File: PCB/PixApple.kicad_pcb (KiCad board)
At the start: 2 copper layers, 100 x 100 mm, 0 parts

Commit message: Routing PCB
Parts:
- added C1: 10u, Capacitor_SMD:C_0603_1608Metric_Pad1.08x0.95mm_HandSolder, F.Cu at (203.7, 97.6)
- added C10: 1u, Capacitor_SMD:C_0603_1608Metric_Pad1.08x0.95mm_HandSolder, F.Cu at (98.1, 76.5)
- added C11: 1u, Capacitor_SMD:C_0603_1608Metric_Pad1.08x0.95mm_HandSolder, F.Cu at (90.0, 74.0)
- added C12: 100n, Capacitor_SMD:C_0603_1608Metric_Pad1.08x0.95mm_HandSolder, F.Cu at (112.1, 91.8)
- added C13: 100n, Capacitor_SMD:C_0603_1608Metric_Pad1.08x0.95mm_HandSolder, F.Cu at (101.4, 87.0)
- added C14: 100n, Capacitor_SMD:C_0603_1608Metric_Pad1.08x0.95mm_HandSolder, F.Cu at (193.8, 107.8)
- added C15: 15p, Capacitor_SMD:C_0603_1608Metric_Pad1.08x0.95mm_HandSolder, F.Cu at (193.6, 132.3)
- added C16: 15p, Capacitor_SMD:C_0603_1608Metric_Pad1.08x0.95mm_HandSolder, F.Cu at (193.6, 127.3)
- added C17: 100n, Capacitor_SMD:C_0603_1608Metric_Pad1.08x0.95mm_HandSolder, F.Cu at (99.9, 108.0)
- added C18: 100n, Capacitor_SMD:C_0603_1608Metric_Pad1.08x0.95mm_HandSolder, F.Cu at (219.4, 117.8)
- added C19: 30p, Capacitor_SMD:C_0603_1608Metric_Pad1.08x0.95mm_HandSolder, F.Cu at (105.5, 100.3)
- added C2: 10u, Capacitor_SMD:C_0603_1608Metric_Pad1.08x0.95mm_HandSolder, F.Cu at (208.1, 101.9)
- added C20: 30p, Capacitor_SMD:C_0603_1608Metric_Pad1.08x0.95mm_HandSolder, F.Cu at (105.5, 102.8)
- added C21: 4.7n, Capacitor_SMD:C_0603_1608Metric_Pad1.08x0.95mm_HandSolder, F.Cu at (227.2, 135.7)
- added C22: 100n, Capacitor_SMD:C_0603_1608Metric_Pad1.08x0.95mm_HandSolder, F.Cu at (239.2, 128.1)
- added C23: 1u, Capacitor_SMD:C_0603_1608Metric_Pad1.08x0.95mm_HandSolder, F.Cu at (240.8, 128.1)
- added C24: 100n, Capacitor_SMD:C_0603_1608Metric_Pad1.08x0.95mm_HandSolder, F.Cu at (219.4, 121.0)
- added C25: 1n, Capacitor_SMD:C_0603_1608Metric_Pad1.08x0.95mm_HandSolder, F.Cu at (219.4, 119.4)
- added C3: 100n, Capacitor_SMD:C_0603_1608Metric_Pad1.08x0.95mm_HandSolder, F.Cu at (105.5, 75.8)
- added C4: 100n, Capacitor_SMD:C_0603_1608Metric_Pad1.08x0.95mm_HandSolder, F.Cu at (111.8, 78.8)
- added C5: 100n, Capacitor_SMD:C_0603_1608Metric_Pad1.08x0.95mm_HandSolder, F.Cu at (97.4, 82.5)
- added C6: 100n, Capacitor_SMD:C_0603_1608Metric_Pad1.08x0.95mm_HandSolder, F.Cu at (103.9, 69.2)
- added C7: 100n, Capacitor_SMD:C_0603_1608Metric_Pad1.08x0.95mm_HandSolder, F.Cu at (96.2, 89.2)
- added C8: 100n, Capacitor_SMD:C_0603_1608Metric_Pad1.08x0.95mm_HandSolder, F.Cu at (101.5, 101.2)
- added C9: 100n, Capacitor_SMD:C_0603_1608Metric_Pad1.08x0.95mm_HandSolder, F.Cu at (111.6, 85.5)
- added D1: 1N4148W, Diode_SMD:D_SOD-123, F.Cu at (223.6, 118.2)
- added D2: LED_Small, LED_SMD:LED_0603_1608Metric_Pad1.05x0.95mm_HandSolder, F.Cu at (134.5, 123.5)
- added D3: LED_Small, LED_SMD:LED_0603_1608Metric_Pad1.05x0.95mm_HandSolder, F.Cu at (135.9, 134.0)
- added J1: USB_C_Receptacle_USB2.0_16P, Connector_USB:USB_C_Plug_Molex_105444, F.Cu at (189.2, 86.0)
- added J10: PWM0, Connector_PinHeader_2.54mm:PinHeader_1x03_P2.54mm_Vertical, F.Cu at (270.6, 84.0)
- added J11: PWM1, Connector_PinHeader_2.54mm:PinHeader_1x03_P2.54mm_Vertical, F.Cu at (270.6, 78.5)
- added J12: PWM2, Connector_PinHeader_2.54mm:PinHeader_1x03_P2.54mm_Vertical, F.Cu at (270.6, 73.0)
- added J13: PWM3, Connector_PinHeader_2.54mm:PinHeader_1x03_P2.54mm_Vertical, F.Cu at (270.6, 67.5)
- added J14: Conn_01x03_Pin, Connector_PinHeader_2.54mm:PinHeader_1x03_P2.54mm_Vertical, F.Cu at (25.0, 131.2)
- added J15: Conn_01x03_Pin, Connector_PinHeader_2.54mm:PinHeader_1x03_P2.54mm_Vertical, F.Cu at (25.0, 125.0)
- added J16: Conn_01x03_Pin, Connector_PinHeader_2.54mm:PinHeader_1x03_P2.54mm_Vertical, F.Cu at (34.7, 148.0)
- added J17: Conn_01x03_Pin, Connector_PinHeader_2.54mm:PinHeader_1x03_P2.54mm_Vertical, F.Cu at (34.7, 143.4)
- added J18: Conn_01x03_Pin, Connector_PinHeader_2.54mm:PinHeader_1x03_P2.54mm_Vertical, F.Cu at (34.7, 138.8)
- added J19: Conn_01x03_Pin, Connector_PinHeader_2.54mm:PinHeader_1x03_P2.54mm_Vertical, F.Cu at (34.7, 134.2)
- added J2: Conn_01x02_Pin, Connector_PinHeader_2.54mm:PinHeader_1x02_P2.54mm_Vertical, F.Cu at (185.8, 96.2)
- added J20: Conn_01x03_Pin, Connector_PinHeader_2.54mm:PinHeader_1x03_P2.54mm_Vertical, F.Cu at (34.7, 129.6)
- added J21: Conn_01x03_Pin, Connector_PinHeader_2.54mm:PinHeader_1x03_P2.54mm_Vertical, F.Cu at (34.7, 125.0)
- added J22: Conn_01x03_Pin, Connector_PinHeader_2.54mm:PinHeader_1x03_P2.54mm_Vertical, F.Cu at (44.4, 148.0)
- added J23: Conn_01x03_Pin, Connector_PinHeader_2.54mm:PinHeader_1x03_P2.54mm_Vertical, F.Cu at (44.4, 143.4)
- added J24: Conn_01x03_Pin, Connector_PinHeader_2.54mm:PinHeader_1x03_P2.54mm_Vertical, F.Cu at (44.4, 138.8)
- added J25: Conn_01x03_Pin, Connector_PinHeader_2.54mm:PinHeader_1x03_P2.54mm_Vertical, F.Cu at (44.4, 134.2)
- added J26: Conn_01x03_Pin, Connector_PinHeader_2.54mm:PinHeader_1x03_P2.54mm_Vertical, F.Cu at (72.0, 136.0)
- added J27: Conn_01x03_Pin, Connector_PinHeader_2.54mm:PinHeader_1x03_P2.54mm_Vertical, F.Cu at (82.0, 124.0)
- added J5: Conn_01x05_Pin, Connector_PinHeader_2.54mm:PinHeader_1x05_P2.54mm_Vertical, F.Cu at (120.2, 69.4)
- added J6: Conn_01x02_Pin, Connector_PinHeader_2.54mm:PinHeader_1x02_P2.54mm_Vertical, F.Cu at (225.9, 140.1)
- added J7: Conn_01x01_Pin, TestPoint:TestPoint_Pad_1.0x1.0mm, F.Cu at (243.0, 118.5)
- added J8: Conn_02x03_Odd_Even, Connector_PinHeader_2.54mm:PinHeader_2x03_P2.54mm_Vertical, F.Cu at (72.5, 68.5)
- added J9: Conn_01x04_Pin, Connector_PinHeader_2.54mm:PinHeader_1x04_P2.54mm_Vertical, F.Cu at (145.0, 73.9)
- added R1: 10k, Resistor_SMD:R_0603_1608Metric_Pad0.98x0.95mm_HandSolder, F.Cu at (190.4, 107.8)
- added R10: 10k, Resistor_SMD:R_0603_1608Metric_Pad0.98x0.95mm_HandSolder, F.Cu at (236.0, 126.3)
- added R11: 60R, Resistor_SMD:R_0603_1608Metric_Pad0.98x0.95mm_HandSolder, F.Cu at (228.0, 132.3)
- added R12: 60R, Resistor_SMD:R_0603_1608Metric_Pad0.98x0.95mm_HandSolder, F.Cu at (226.4, 132.3)
- added R13: 220R, Resistor_SMD:R_0603_1608Metric_Pad0.98x0.95mm_HandSolder, F.Cu at (92.6, 79.2)
- added R14: 220R, Resistor_SMD:R_0603_1608Metric_Pad0.98x0.95mm_HandSolder, F.Cu at (99.1, 94.6)
- added R2: 1k, Resistor_SMD:R_0603_1608Metric_Pad0.98x0.95mm_HandSolder, F.Cu at (187.0, 107.8)
- added R3: 1k, Resistor_SMD:R_0603_1608Metric_Pad0.98x0.95mm_HandSolder, F.Cu at (196.6, 128.4)
- added R4: 27R, Resistor_SMD:R_0603_1608Metric_Pad0.98x0.95mm_HandSolder, F.Cu at (104.0, 81.8)
- added R5: 27R, Resistor_SMD:R_0603_1608Metric_Pad0.98x0.95mm_HandSolder, F.Cu at (107.0, 89.2)
- added R6: 10k, Resistor_SMD:R_0603_1608Metric_Pad0.98x0.95mm_HandSolder, F.Cu at (95.5, 68.5)
- added R7: 1k, Resistor_SMD:R_0603_1608Metric_Pad0.98x0.95mm_HandSolder, F.Cu at (228.0, 117.8)
- added R8: 10k, Resistor_SMD:R_0603_1608Metric_Pad0.98x0.95mm_HandSolder, F.Cu at (228.0, 119.6)
- added R9: 1k, Resistor_SMD:R_0603_1608Metric_Pad0.98x0.95mm_HandSolder, F.Cu at (114.2, 97.8)
- added SW1: SW_Push, Button_Switch_THT:SW_PUSH_6mm_H5mm, F.Cu at (56.0, 44.8)
- added U1: RP2040, Package_DFN_QFN:QFN-56-1EP_7x7mm_P0.4mm_EP3.2x3.2mm, F.Cu at (195.3, 120.9)
- added U2: NCP1117-3.3_TO252, Package_TO_SOT_SMD:TO-252-2, F.Cu at (203.8, 104.8)
- added U3: W25Q128JVS, Package_SO:SOIC-8_5.3x5.3mm_P1.27mm, F.Cu at (190.3, 111.5)
- added U4: SN65HVD230DR, SN65HVD230DR:SOIC127P599X175-8N, F.Cu at (238.0, 122.7)
- added U5: MCP2515-xSO, Package_SO:SOIC-18W_7.5x11.6mm_P1.27mm, F.Cu at (235.8, 113.9)
- added Y1: ABM8-272-T3, ABM8-272-T3:XTAL_ABM8-272-T3, F.Cu at (193.6, 129.8)
- added Y2: ABM8-16.000MHZ-B2-T, ABM8-16.000MHZ-B2-T:XTAL_ABM8-16.000MHZ-B2-T, F.Cu at (133.8, 60.0)
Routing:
- net +3V3: track 0.00 -> 70.0 mm, vias 0 -> 2
- net GND: track 0.00 -> 63.6 mm, vias 0 -> 22
- net /storage/QSPI_SS: track 0.00 -> 20.2 mm
- net /storage/QSPI_SD1: track 0.00 -> 15.1 mm
- net Net-(U4-VREF): track 0.00 -> 14.6 mm
- net /storage/QSPI_SD2: track 0.00 -> 13.7 mm
- net Net-(U1-VREG_VOUT): track 0.00 -> 12.8 mm
- net /can/CANH: track 0.00 -> 12.8 mm
- net /can/CANL: track 0.00 -> 12.8 mm
- net Net-(D1-A): track 0.00 -> 12.7 mm
- net Net-(C15-Pad2): track 0.00 -> 9.73 mm
- net /storage/QSPI_SD3: track 0.00 -> 8.35 mm
- net /can/TXCAN: track 0.00 -> 7.87 mm
- net /storage/QSPI_SCLK: track 0.00 -> 6.71 mm
- net Net-(U1-USB_DM): track 0.00 -> 5.92 mm
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- added copper zone on B.Cu, net GND
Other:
- board outline removed

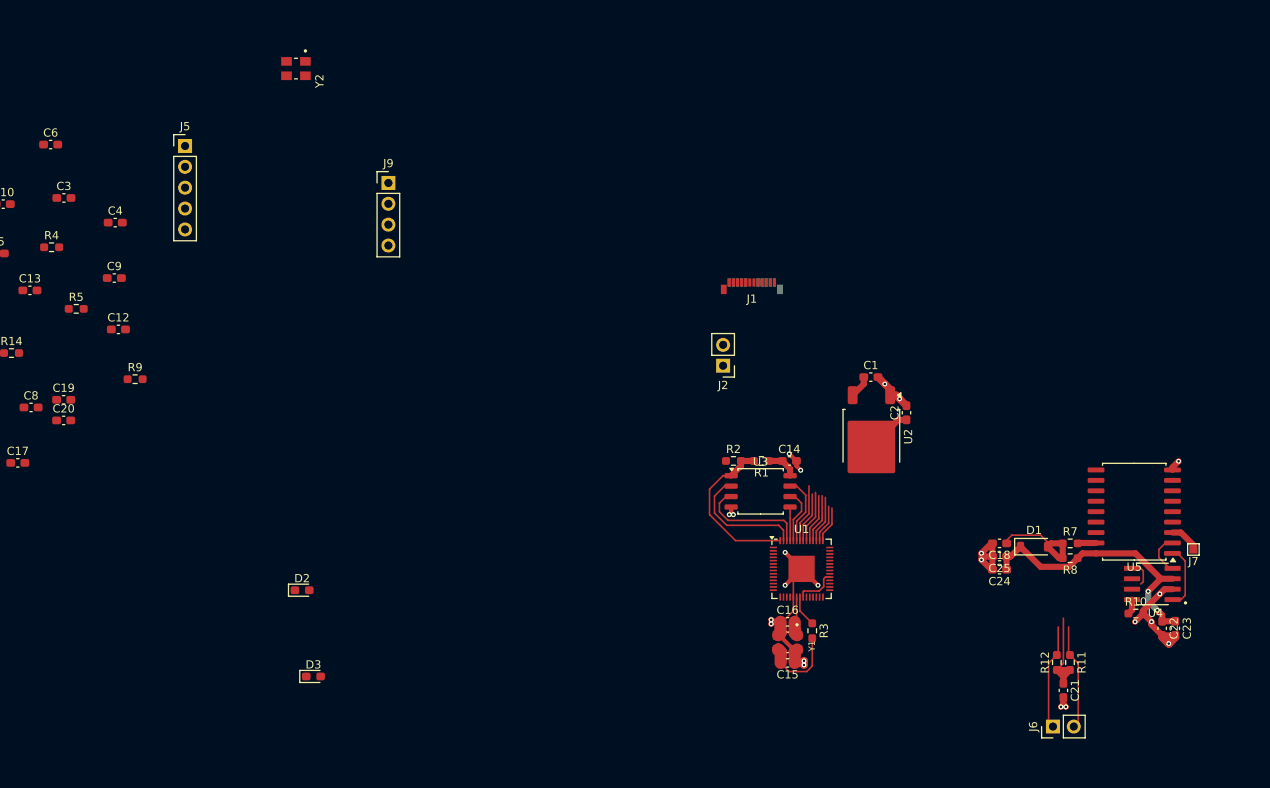
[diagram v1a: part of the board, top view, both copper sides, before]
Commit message: Redo time, pcb too close
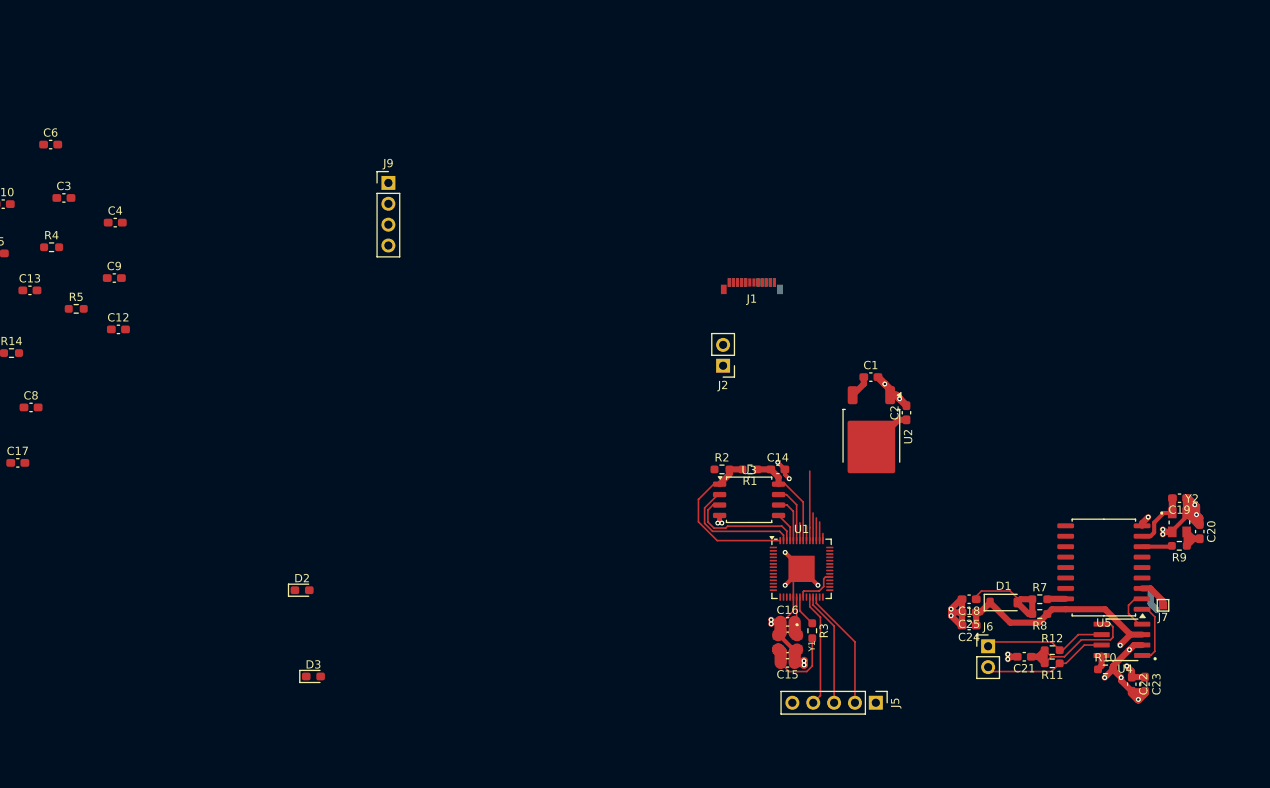
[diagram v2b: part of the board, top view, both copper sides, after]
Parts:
- J10: value PWM0 -> Conn_01x03_Pin
- J11: value PWM1 -> Conn_01x03_Pin
- J12: value PWM2 -> Conn_01x03_Pin
- J13: value PWM3 -> Conn_01x03_Pin
- moved C20 139.0 mm to (243.8, 116.4), turned to -90 degrees
- moved C19 136.4 mm to (241.3, 112.3), turned to 180 degrees
- moved R9 128.7 mm to (241.3, 118.1), turned to 180 degrees
- moved Y2 120.9 mm to (241.3, 115.2), turned to 0 degrees
- moved J5 108.0 mm to (204.3, 137.2), turned to -90 degrees
- moved J6 12.6 mm to (218.0, 130.3), turned to 0 degrees
- moved C23 7.74 mm to (237.1, 134.9)
- moved C18 7.74 mm to (215.7, 124.6)
- moved C24 7.74 mm to (215.7, 127.8)
- moved C25 7.74 mm to (215.7, 126.2)
- moved U5 7.74 mm to (232.1, 120.7)
- moved C22 7.74 mm to (235.5, 134.9)
- moved R8 7.74 mm to (224.3, 126.4)
- moved D1 7.74 mm to (219.9, 125.0)
- moved J7 7.74 mm to (239.3, 125.3)
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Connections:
- C20 pad 2: GND -> Net-(C20-Pad2)
- R9 pad 1: GND -> Net-(C20-Pad2)
- Y2 pad 3: GND -> Net-(C20-Pad2)
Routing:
- net GND: track 63.6 -> 81.5 mm, vias 22 -> 26
- net /RESET: track 0.00 -> 14.8 mm
- net /SWD: track 0.00 -> 13.9 mm
- net /SWCLK: track 0.00 -> 13.8 mm
- net +3V3: track 70.0 -> 61.8 mm
- net Net-(U1-VREG_VOUT): track 12.8 -> 4.93 mm
- net Net-(U5-OSC1): track 0.00 -> 7.36 mm
- net Net-(C20-Pad2): track 0.00 -> 4.89 mm
- net Net-(U4-VREF): track 14.6 -> 18.2 mm
- net Net-(U5-OSC2): track 0.00 -> 3.67 mm
- net /can/CANH: track 12.8 -> 15.6 mm
- net /can/CANL: track 12.8 -> 15.5 mm
- net Net-(U1-USB_DM): track 5.92 -> 3.36 mm
- net Net-(U1-USB_DP): track 5.92 -> 8.46 mm
- net /storage/QSPI_SD3: track 8.35 -> 7.08 mm
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
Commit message: PCB routing, better placement
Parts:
- removed C5: 100n, Capacitor_SMD:C_0603_1608Metric_Pad1.08x0.95mm_HandSolder
- added J28: Conn_01x01_Pin, TestPoint:TestPoint_Pad_1.0x1.0mm, F.Cu at (203.0, 72.5)
- added J29: Conn_01x01_Pin, TestPoint:TestPoint_Pad_1.0x1.0mm, F.Cu at (203.0, 70.2)
- added J3: Conn_01x01_Pin, TestPoint:TestPoint_Pad_1.0x1.0mm, F.Cu at (184.4, 60.6)
- added J30: Conn_01x01_Pin, TestPoint:TestPoint_Pad_1.0x1.0mm, F.Cu at (203.0, 68.0)
- added J4: Conn_01x01_Pin, TestPoint:TestPoint_Pad_1.0x1.0mm, F.Cu at (186.8, 60.6)
- C25: value 1n -> 1u
- moved J10 258.7 mm to (20.1, 19.3), turned to 0 degrees
- moved J11 252.9 mm to (24.6, 19.3), turned to 0 degrees
- moved J12 247.2 mm to (29.2, 19.3), turned to 0 degrees
- moved J13 241.6 mm to (33.8, 19.3), turned to 0 degrees
- moved D3 126.7 mm to (41.0, 49.9)
- moved J16 119.8 mm to (20.1, 29.0), turned to 0 degrees
- moved J17 114.8 mm to (24.6, 29.0), turned to 0 degrees
- moved J14 112.6 mm to (38.4, 19.3), turned to 0 degrees
- moved J22 111.9 mm to (20.1, 38.7), turned to 0 degrees
- moved J18 109.9 mm to (29.2, 29.0), turned to 0 degrees
- moved J15 107.2 mm to (43.0, 19.3), turned to 0 degrees
- moved J23 106.5 mm to (24.6, 38.7), turned to 0 degrees
- moved J19 105.2 mm to (33.8, 29.0), turned to 0 degrees
- moved J26 102.9 mm to (38.4, 38.7), turned to 0 degrees
- moved J24 101.2 mm to (29.2, 38.7), turned to 0 degrees
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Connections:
- U1 pad 27: Net-(D2-A) -> /SPI0_RX
- U1 pad 28: /CAN_INT -> /SPI0_CSn
- U1 pad 31: /SPI0_RX -> /CAN_INT
- U1 pad 32: /SPI0_CSn -> Net-(D2-A)
- U5 pad 10: unconnected-(U5-~{RX1BF}-Pad10) -> /can/RX1BF
- U5 pad 11: unconnected-(U5-~{RX0BF}-Pad11) -> /can/RX0BF
- U5 pad 4: unconnected-(U5-~{TX0RTS}-Pad4) -> /can/TX0RTS
- U5 pad 5: unconnected-(U5-~{TX1RTS}-Pad5) -> /can/TX1RTS
- U5 pad 6: unconnected-(U5-~{TX2RTS}-Pad6) -> /can/TX2RTS
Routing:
- net +3V3: track 61.8 -> 106.4 mm, vias 2 -> 0
- net GND: track 81.5 -> 118.6 mm, vias 26 -> 49
- net /I2C1_SDA: track 0.00 -> 26.9 mm
- net /I2C1_SCL: track 0.00 -> 24.1 mm
- net /SPI0_RX: track 0.00 -> 19.5 mm
- net /SPI0_CSn: track 0.00 -> 19.5 mm, vias 0 -> 2
- net Net-(U4-VREF): track 18.2 -> 36.9 mm, vias 0 -> 2
- net /SPI0_TX: track 0.00 -> 18.1 mm, vias 0 -> 2
- net /SPI0_SCK: track 0.00 -> 17.6 mm
- net /CAN_INT: track 0.00 -> 17.5 mm
- net VBUS: track 2.76 -> 16.5 mm
- net Net-(U1-VREG_VOUT): track 4.93 -> 14.1 mm
- net /RESET: track 14.8 -> 23.4 mm
- net /SWD: track 13.9 -> 22.3 mm
- net /can/TX0RTS: track 0.00 -> 7.86 mm
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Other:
- board outline added: 100 x 100 mm

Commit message: Finished PCB routing
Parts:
- removed C13, C8, C9: 100n, Capacitor_SMD:C_0603_1608Metric_Pad1.08x0.95mm_HandSolder
- removed J12, J13, J14, J15, J16, J17, J18, J19, J20, J21, J22, J23, J24, J25, J26, J27: Conn_01x03_Pin, Connector_PinHeader_2.54mm:PinHeader_1x03_P2.54mm_Vertical
- added C5: 100n, Capacitor_SMD:C_0603_1608Metric_Pad1.08x0.95mm_HandSolder, F.Cu at (144.3, 56.9)
- added M3: MountingHole_3.2mm_M3, MountingHole:MountingHole_3.2mm_M3, F.Cu at (117.5, 35.0)
- added M3: MountingHole_3.2mm_M3, MountingHole:MountingHole_3.2mm_M3, F.Cu at (117.5, 95.0)
- added M3: MountingHole_3.2mm_M3, MountingHole:MountingHole_3.2mm_M3, F.Cu at (205.0, 35.0)
- added M3: MountingHole_3.2mm_M3, MountingHole:MountingHole_3.2mm_M3, F.Cu at (205.0, 95.0)
- added R15: 5.1K, Resistor_SMD:R_0603_1608Metric_Pad0.98x0.95mm_HandSolder, F.Cu at (152.9, 42.0)
- added R16: 5.1K, Resistor_SMD:R_0603_1608Metric_Pad0.98x0.95mm_HandSolder, F.Cu at (157.1, 42.0)
- added R17: 1k, Resistor_SMD:R_0603_1608Metric_Pad0.98x0.95mm_HandSolder, F.Cu at (162.7, 83.9)
- added R18: 1k, Resistor_SMD:R_0603_1608Metric_Pad0.98x0.95mm_HandSolder, F.Cu at (139.6, 37.9)
- added R19: 4.7K, Resistor_SMD:R_0603_1608Metric_Pad0.98x0.95mm_HandSolder, F.Cu at (145.1, 69.7)
- added R20: 4.7K, Resistor_SMD:R_0603_1608Metric_Pad0.98x0.95mm_HandSolder, F.Cu at (147.6, 69.7)
- added SW2: SW_Push, Button_Switch_THT:SW_PUSH_6mm, F.Cu at (135.3, 42.9)
- J1: footprint Connector_USB:USB_C_Plug_Molex_105444 -> Connector_USB:USB_C_Receptacle_GCT_USB4105-xx-A_16P_TopMnt_Horizontal
- J10, J11: value Conn_01x03_Pin -> Conn_01x11; footprint Connector_PinHeader_2.54mm:PinHeader_1x03_P2.54mm_Vertical -> Connector_PinHeader_2.54mm:PinHeader_1x11_P2.54mm_Vertical
- SW1: footprint Button_Switch_THT:SW_PUSH_6mm_H5mm -> Button_Switch_THT:SW_PUSH_6mm
- moved J10 181.1 mm to (199.8, 41.2), turned to -90 degrees
- moved D3 153.0 mm to (193.9, 54.9)
- moved R14 140.7 mm to (193.9, 57.1)
- moved SW1 131.3 mm to (172.6, 88.2), turned to 180 degrees
- moved C17 119.2 mm to (163.9, 71.5)
- moved R6 119.1 mm to (163.9, 74.2), turned to 180 degrees
- moved C7 118.2 mm to (162.5, 55.4)
- moved J8 118.1 mm to (136.6, 67.2)
- moved J11 108.1 mm to (129.1, 47.2)
- moved C6 99.7 mm to (143.7, 51.8), turned to 180 degrees
- moved D2 27.0 mm to (192.9, 46.1), turned to 90 degrees
- moved R13 25.8 mm to (194.9, 46.1), turned to -90 degrees
- moved J4 17.8 mm to (170.9, 52.5)
- moved J3 17.2 mm to (168.6, 53.7)
- moved C21 17.1 mm to (183.1, 83.2)
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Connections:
- net /storage/QSPI_SS renamed /QSPI_RST
- C11 pad 1: Net-(U1-VREG_VOUT) -> +1V1
- C12 pad 2: Net-(U1-VREG_VOUT) -> GND
- C17 pad 1: Net-(C17-Pad1) -> /RESET
- J1 pad A5: unconnected-(J1-CC1-PadA5) -> Net-(J1-CC1)
- J1 pad B5: unconnected-(J1-CC2-PadB5) -> Net-(J1-CC2)
- J10 pad 1: GND -> VBUS
- J11 pad 1: GND -> VBUS
- J11 pad 3: /PWM1 -> /GPIO0
- SW1 pad 1: Net-(C17-Pad1) -> GND
- SW1 pad 2: /RESET -> Net-(R17-Pad1)
- U1 pad 17: /I2C1_SDA -> Net-(U1-GPIO14)
- U1 pad 18: /I2C1_SCL -> Net-(U1-GPIO15)
- U1 pad 23: Net-(U1-VREG_VOUT) -> +1V1
- U1 pad 45: Net-(U1-VREG_VOUT) -> +1V1
- U1 pad 50: Net-(U1-VREG_VOUT) -> +1V1
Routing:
- net +3V3: track 106.4 -> 396.1 mm, vias 0 -> 2
- net VBUS: track 16.5 -> 277.1 mm, vias 0 -> 2
- net GND: track 118.6 -> 168.4 mm, vias 49 -> 65
- net /PWM0: track 0.00 -> 43.6 mm
- net /PWM1: track 0.00 -> 40.9 mm
- net /PWM2: track 0.00 -> 38.6 mm
- net Net-(D2-A): track 4.16 -> 41.8 mm
- net /PWM3: track 0.00 -> 36.5 mm
- net /ADC0: track 0.00 -> 34.0 mm
- net /ADC1: track 0.00 -> 30.6 mm
- net /ADC2: track 0.00 -> 29.0 mm
- net /GPIO7: track 0.00 -> 27.6 mm
- net /ADC3: track 0.00 -> 27.3 mm
- net /SPI1_TX: track 0.00 -> 26.2 mm
- net /GPIO6: track 0.00 -> 26.2 mm
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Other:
- board size 100 x 100 mm -> 97.5 x 70 mm

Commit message: labeling done
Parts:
- moved R17 4.04 mm to (162.7, 87.9), turned to -90 degrees
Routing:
- net /RESET: track 31.2 -> 36.0 mm
- net Net-(R17-Pad1): track 10.4 -> 11.3 mm
- net GND: track 168.4 -> 168.9 mm, vias 65 -> 66
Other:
- board text added: "+3V3"
- board text added: "+5V"
- board text added: "ADC0"
- board text added: "ADC1"
- board text added: "ADC2"
- board text added: "ADC3"
- board text added: "CAN"
- board text added: "CANH (G)"
- board text added: "CANL (Y)"
- board text added: "CSn"
- board text added: "DEBUG"
- board text added: "GND"
- board text added: "GPIO0"
- board text added: "GPIO1"
- board text added: "GPIO2"
- board text added: "GPIO3"
- board text added: "GPIO4"
- board text added: "GPIO5"
- board text added: "GPIO6"
- board text added: "GPIO7"
- board text added: "I2C"
- board text added: "PWM0"
- board text added: "PWM1"
- board text added: "PWM2"
- board text added: "PWM3"
- board text added: "RESET"
- board text added: "RST"
- board text added: "RX"
- board text added: "SCK"
- board text added: "SCL"
- board text added: "SDA"
- board text added: "SPI"
- board text added: "SWCLK"
- board text added: "SWD"
- board text added: "TX"

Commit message: Writeup + case
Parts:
- added +3V3: TestPoint_Pad_2.0x2.0mm, TestPoint:TestPoint_Pad_2.0x2.0mm, F.Cu at (129.2, 32.5)
- added D4: 1N5819WS, Diode_SMD:D_SOD-323, F.Cu at (159.4, 40.6)
- added D5: 1N5819WS, Diode_SMD:D_SOD-323, F.Cu at (170.0, 33.2)
- added G***: LOGO, LOGO, F.Cu at (118.5, 44.5)
- added G***: LOGO, LOGO, B.Cu at (184.9, 78.0)
- added G***: LOGO, LOGO, B.Cu at (152.6, 55.5)
- added GND: TestPoint_Pad_2.0x2.0mm, TestPoint:TestPoint_Pad_2.0x2.0mm, F.Cu at (134.2, 32.5)
- added J12: Conn_01x02_Pin, Connector_PinHeader_2.54mm:PinHeader_1x02_P2.54mm_Vertical, F.Cu at (174.3, 33.2)
- moved C1 2.64 mm to (159.4, 44.6), turned to -90 degrees
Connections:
- J1 pad A4: VBUS -> Net-(D4-A)
- J1 pad A9: VBUS -> Net-(D4-A)
- J1 pad B4: VBUS -> Net-(D4-A)
- J1 pad B9: VBUS -> Net-(D4-A)
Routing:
- net VBUS: track 277.1 -> 215.3 mm
- net Net-(D4-A): track 0.00 -> 10.2 mm
- net GND: track 168.9 -> 172.7 mm, vias 66 -> 92
- net /usb/USB_D-: track 8.55 -> 12.2 mm
- net +3V3: track 396.1 -> 399.5 mm
- net Net-(D5-A): track 0.00 -> 3.25 mm
- net /usb/USB_D+: track 9.09 -> 11.6 mm
- added copper zone on F.Cu, net GND
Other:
- board text added: "Flash"
- board text added: "JLCJLCJLCJLC"
- board text added: "PixApple V1.0"
- board text added: "QA"
